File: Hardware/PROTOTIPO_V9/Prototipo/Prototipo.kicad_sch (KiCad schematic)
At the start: 1 part, among them U1 YAAJ_BluePill_Part_Like_SWD_B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

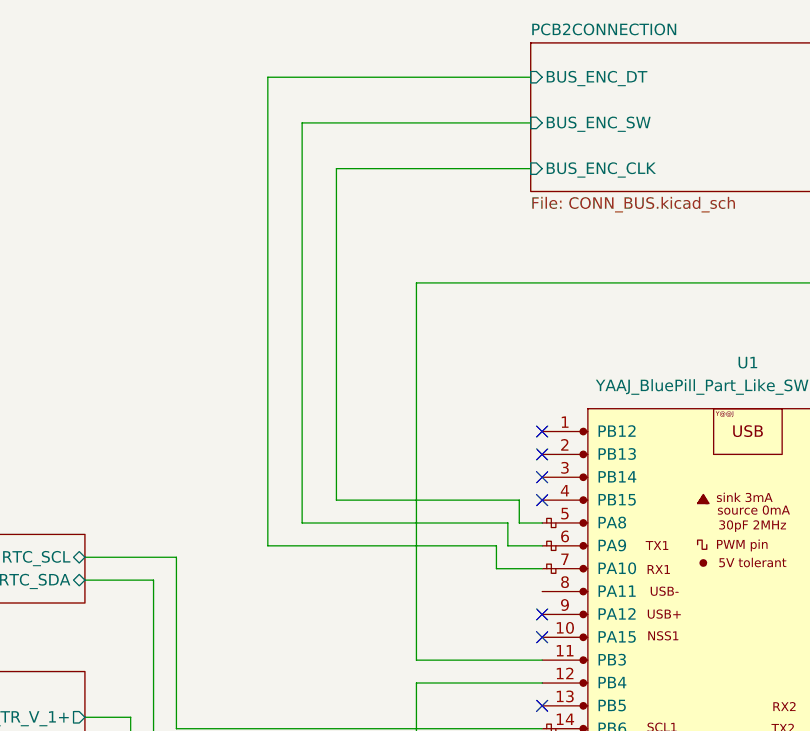
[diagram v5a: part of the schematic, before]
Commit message: Footprints asignados
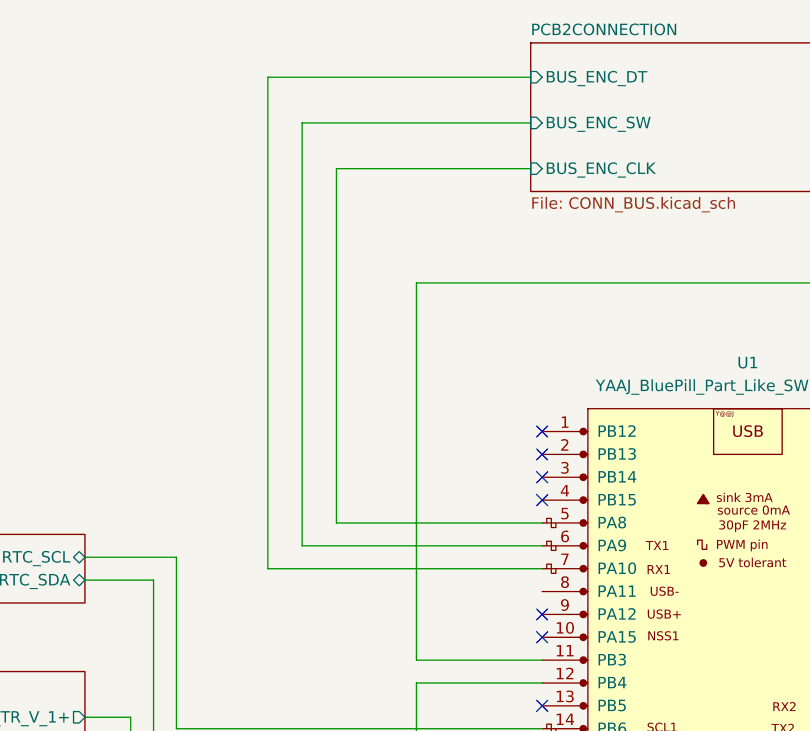
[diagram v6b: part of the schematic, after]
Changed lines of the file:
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@@
 	(wire
 		(pts
-			(xy 101.6 46.99) (xy 101.6 83.82)
+			(xy 101.6 46.99) (xy 101.6 86.36)
 		)
 		(stroke
@@
 	(wire
 		(pts
-			(xy 101.6 83.82) (xy 121.92 83.82)
-		)
-		(stroke
-			(width 0)
-			(type default)
-		)
-	)
-	(wire
-		(pts
-			(xy 93.98 36.83) (xy 93.98 88.9)
+			(xy 101.6 86.36) (xy 124.46 86.36)
+		)
+		(stroke
+			(width 0)
+			(type default)
+		)
+	)
+	(wire
+		(pts
+			(xy 93.98 36.83) (xy 93.98 91.44)
 		)
 		(stroke
@@
 	(wire
 		(pts
-			(xy 120.65 86.36) (xy 97.79 86.36)
+			(xy 97.79 88.9) (xy 124.46 88.9)
 		)
 		(stroke
@@
 	(wire
 		(pts
-			(xy 121.92 86.36) (xy 124.46 86.36)
-		)
-		(stroke
-			(width 0)
-			(type default)
-		)
-	)
-	(wire
-		(pts
 			(xy 76.2 137.16) (xy 73.66 137.16)
 		)
@@
 	(wire
 		(pts
-			(xy 120.65 88.9) (xy 120.65 86.36)
-		)
-		(stroke
-			(width 0)
-			(type default)
-		)
-	)
-	(wire
-		(pts
 			(xy 73.66 90.17) (xy 83.82 90.17)
 		)
@@
 	(wire
 		(pts
-			(xy 93.98 88.9) (xy 119.38 88.9)
+			(xy 93.98 91.44) (xy 124.46 91.44)
 		)
 		(stroke
@@
 	(wire
 		(pts
-			(xy 121.92 83.82) (xy 121.92 86.36)
-		)
-		(stroke
-			(width 0)
-			(type default)
-		)
-	)
-	(wire
-		(pts
 			(xy 78.74 139.7) (xy 78.74 158.75)
 		)
@@
 	(wire
 		(pts
-			(xy 119.38 91.44) (xy 124.46 91.44)
-		)
-		(stroke
-			(width 0)
-			(type default)
-		)
-	)
-	(wire
-		(pts
 			(xy 73.66 134.62) (xy 78.74 134.62)
 		)
@@
 	(wire
 		(pts
-			(xy 124.46 88.9) (xy 120.65 88.9)
-		)
-		(stroke
-			(width 0)
-			(type default)
-		)
-	)
-	(wire
-		(pts
 			(xy 170.18 96.52) (xy 175.26 96.52)
 		)
@@
 	(wire
 		(pts
-			(xy 119.38 88.9) (xy 119.38 91.44)
-		)
-		(stroke
-			(width 0)
-			(type default)
-		)
-	)
-	(wire
-		(pts
-			(xy 97.79 86.36) (xy 97.79 41.91)
-		)
-		(stroke
+			(xy 97.79 88.9) (xy 97.79 41.91)
+		)
+		(stroke

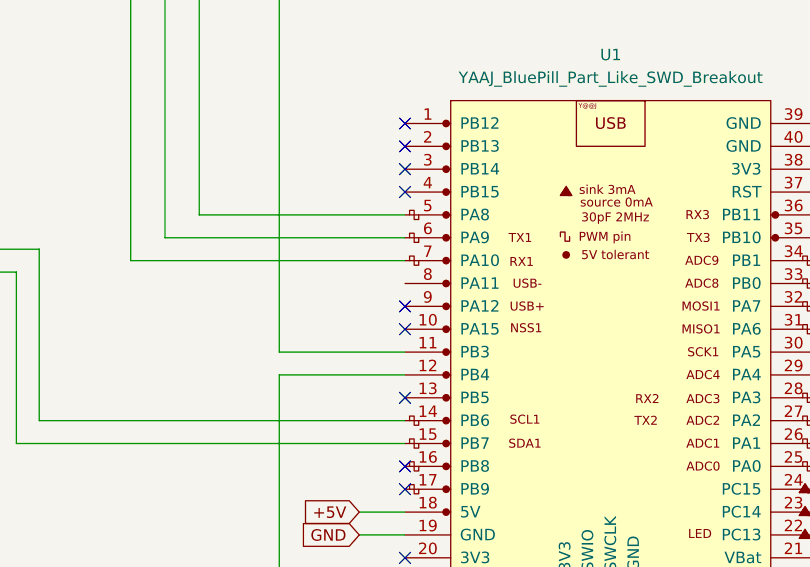
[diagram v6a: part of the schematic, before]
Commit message: Ruteo de PCB Superior
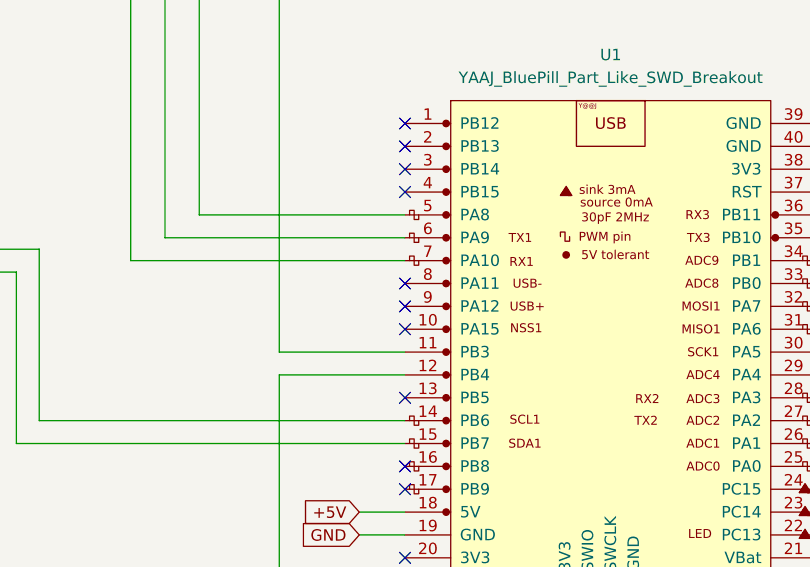
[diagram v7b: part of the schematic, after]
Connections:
- no-connect marks 24 -> 25
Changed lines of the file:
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@@
+	)
+	(no_connect
+		(at 124.46 93.98)
 	)
 	(no_connect

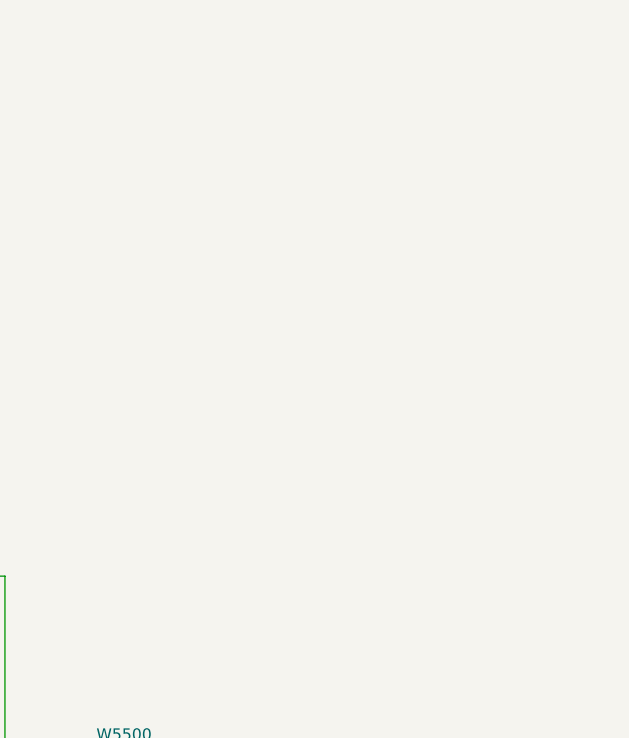
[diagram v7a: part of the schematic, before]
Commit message: Migrar a BlackPill
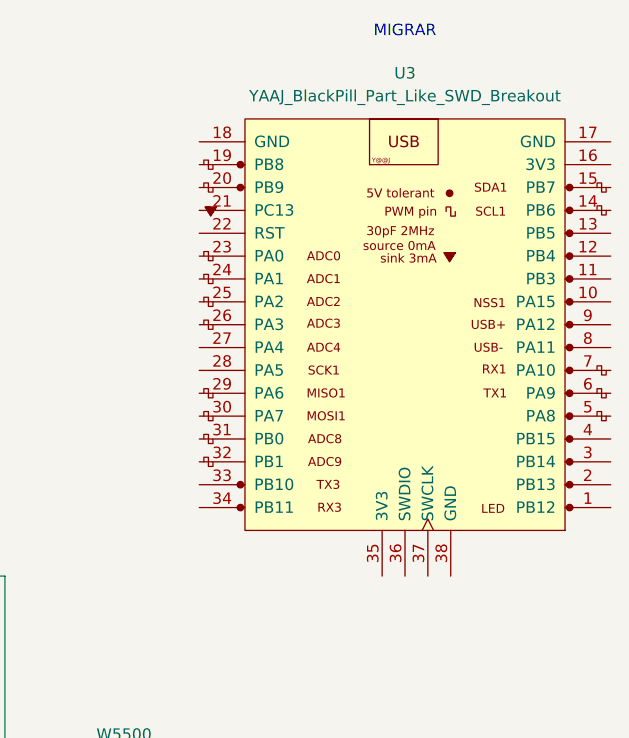
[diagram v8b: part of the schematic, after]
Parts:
- added U3: YAAJ_BlackPill_Part_Like_SWD_Breakout, footprints_proyecto:YAAJ_BlackPill_SWD_1, symbol YAAJ_BlackPill_Part_Like_SWD_Breakout:YAAJ_BlackPill_Part_Like_SWD_Breakout
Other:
- note added: "MIGRAR"
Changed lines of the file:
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@@
 	(generator_version "9.0")
 	(paper "A4")
+	(text "MIGRAR"
+		(exclude_from_sim no)
+		(at 233.68 30.988 0)
+		(effects
+			(font
+				(size 1.27 1.27)
+			)
+		)
+	)
 	(junction
 		(at 172.72 77.47)
@@
 			)
 		)
+	)
+	(rule_area
+		(polyline
+			(pts
+				(xy 204.47 31.75) (xy 204.47 93.98) (xy 207.01 96.52) (xy 260.35 96.52) (xy 262.89 93.345) (xy 262.89 31.115)
+				(xy 260.35 29.21) (xy 207.01 29.21)
+			)
+			(stroke
+				(width 0)
+				(type dash)
+			)
+			(fill
+				(type none)
+			)
+		)
+	)
+	(symbol
+		(lib_id "YAAJ_BlackPill_Part_Like_SWD_Breakout:YAAJ_BlackPill_Part_Like_SWD_Breakout")
+		(at 233.68 63.5 180)
+		(unit 1)
+		(exclude_from_sim no)
+		(in_bom yes)
+		(on_board yes)
+		(dnp no)
+		(fields_autoplaced yes)
+		(property "Reference" "U3"
+			(at 233.68 35.56 0)
+			(effects
+				(font
+					(size 1.27 1.27)
+				)
+			)
+		)
+		(property "Value" "YAAJ_BlackPill_Part_Like_SWD_Breakout"
+			(at 233.68 38.1 0)
+			(effects
+				(font
+					(size 1.27 1.27)
+				)
+			)
+		)
+		(property "Footprint" "footprints_proyecto:YAAJ_BlackPill_SWD_1"
+			(at 217.17 33.02 0)
+			(effects
+				(font
+					(size 1.27 1.27)
+				)
+				(hide yes)
+			)
+		)
+		(property "Datasheet" ""
+			(at 217.17 33.02 0)
+			(effects
+				(font
+					(size 1.27 1.27)
+				)
+				(hide yes)
+			)
+		)
+		(property "Description" ""
+			(at 233.68 63.5 0)
+			(effects
+				(font
+					(size 1.27 1.27)
+				)
+				(hide yes)
+			)
+		)
+		(pin "3"
+		)
+		(pin "6"
+		)
+		(pin "9"
+		)
+		(pin "4"
+		)
+		(pin "7"
+		)
+		(pin "10"
+		)
+		(pin "12"
+		)
+		(pin "13"
+		)
+		(pin "1"
+		)
+		(pin "14"
+		)
+		(pin "5"
+		)
+		(pin "15"
+		)
+		(pin "8"
+		)
+		(pin "2"
+		)
+		(pin "11"
+		)
+		(pin "20"
+		)
+		(pin "33"
+		)
+		(pin "23"
+		)
+		(pin "34"
+		)
+		(pin "35"
+		)
+		(pin "27"
+		)
+		(pin "25"
+		)
+		(pin "21"
+		)
+		(pin "32"
+		)
+		(pin "16"
+		)
+		(pin "26"
+		)
+		(pin "38"
+		)
+		(pin "37"
+		)
+		(pin "31"
+		)
+		(pin "18"
+		)
+		(pin "22"
+		)
+		(pin "28"
+		)
+		(pin "17"
+		)
+		(pin "36"
+		)
+		(pin "30"
+		)
+		(pin "29"
+		)
+		(pin "24"
+		)
+		(pin "19"
+		)
+		(instances
+			(project ""
+				(path "/f7e5c6e4-37d6-479e-ad19-5d06867b62e9"
+					(reference "U3")
+					(unit 1)
+				)
+			)
+		)
